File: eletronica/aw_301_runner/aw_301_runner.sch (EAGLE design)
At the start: 9 parts, among them IC1 AT90S2313P, Q1 4 Mhz

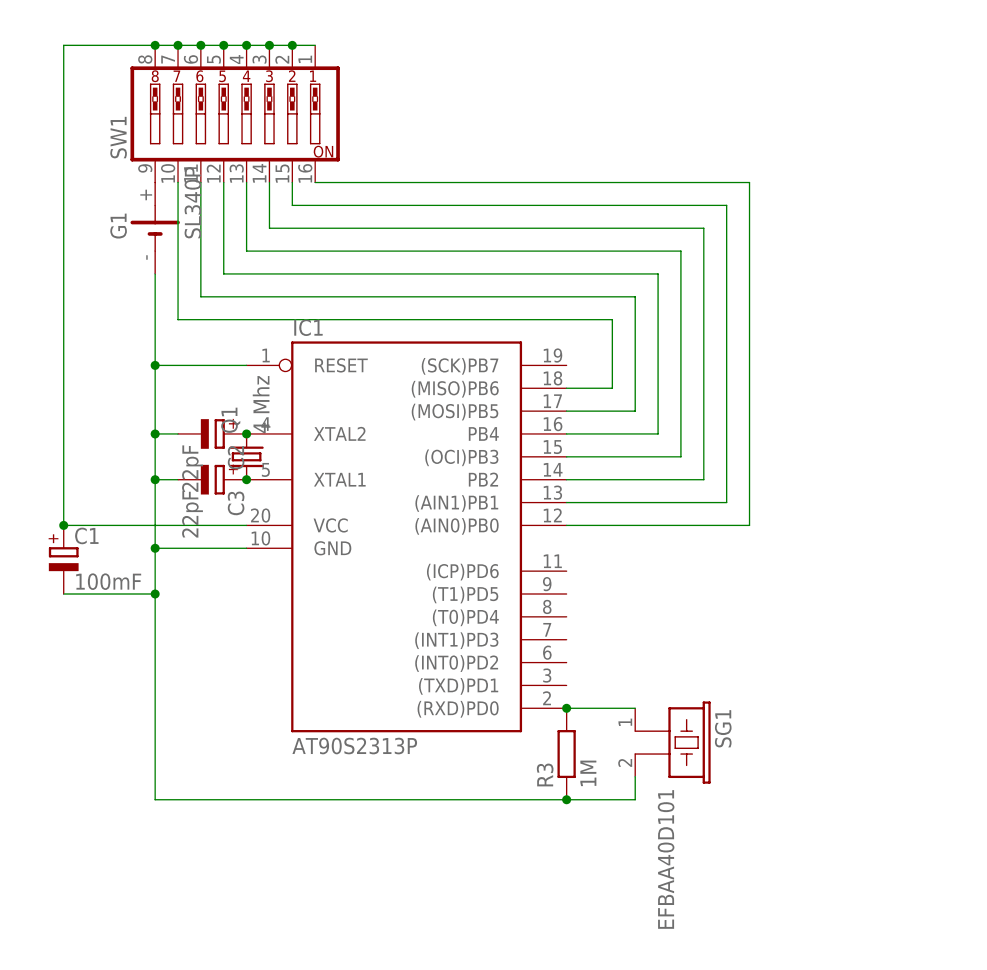
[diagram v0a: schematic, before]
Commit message: 
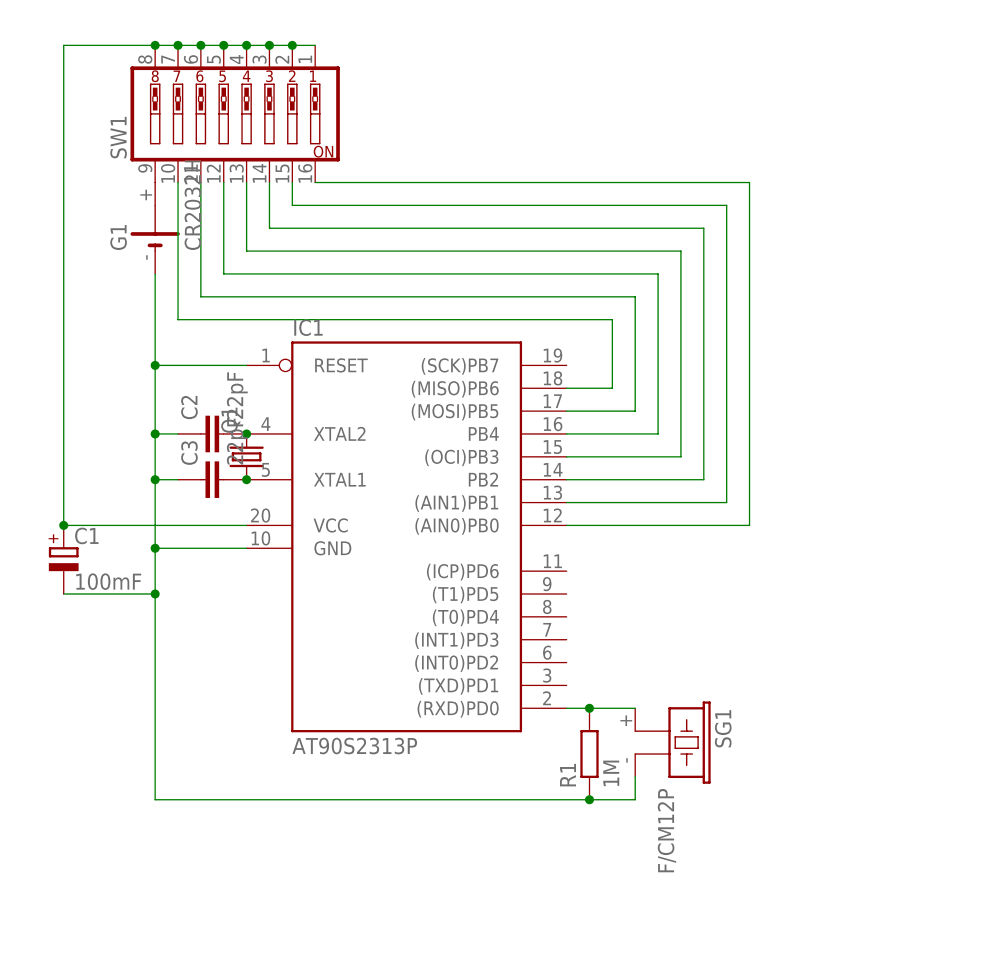
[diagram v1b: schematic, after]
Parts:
- removed R3: 1M, resistor:R-EU_0204/7
- added R1: 1M, rcl:R-EU_0207/10
- C1: device resistor:CPOL-EUE -> resistor:CPOL-EUE2.5-6
- C2, C3: device resistor:CPOL-EUE -> rcl:C-EU025-025X050
- G1: value SL340P -> CR2032H; device battery:SL340P -> battery:CR2032H
- Q1: value 4 Mhz -> (none); device crystal:CRYSTALHC49U-V -> crystal:CRYSTALHC49U70
- SG1: value EFBAA40D101 -> F/CM12P; device buzzer:EFBAA40D101 -> buzzer:F/CM12P
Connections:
- net N$2: now also C2.2; no longer C2.+
- net N$3: now also C3.2; no longer C3.+
- net N$6: now also R1.2; no longer R3.2
- net N$7: now also C2.1, C3.1, R1.1; no longer C2.-, C3.-, R3.1
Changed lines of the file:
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@@
 <part name="IC1" library="atmel" deviceset="AT90S2313" device="P"/>
 <part name="SW1" library="special" deviceset="SW_DIP-8" device=""/>
-<part name="G1" library="battery" deviceset="SL340P" device=""/>
-<part name="Q1" library="crystal" deviceset="CRYSTAL" device="HC49U-V" value="4 Mhz"/>
-<part name="C1" library="resistor" deviceset="CPOL-EU" device="E" value="100mF"/>
-<part name="R3" library="resistor" deviceset="R-EU_" device="0204/7" value="1M"/>
-<part name="SG1" library="buzzer" deviceset="EFB?" device="AA40D101"/>
-<part name="C2" library="resistor" deviceset="CPOL-EU" device="E" value="22pF"/>
-<part name="C3" library="resistor" deviceset="CPOL-EU" device="E" value="22pF"/>
+<part name="G1" library="battery" deviceset="CR2032H" device=""/>
+<part name="SG1" library="buzzer" deviceset="F/CM12P" device=""/>
+<part name="C1" library="resistor" deviceset="CPOL-EU" device="E2.5-6" value="100mF"/>
+<part name="Q1" library="crystal" deviceset="CRYSTAL" device="HC49U70"/>
+<part name="C2" library="rcl" deviceset="C-EU" device="025-025X050" value="22pF"/>
+<part name="C3" library="rcl" deviceset="C-EU" device="025-025X050" value="22pF"/>
+<part name="R1" library="rcl" deviceset="R-EU_" device="0207/10" value="1M"/>
 </parts>
 <sheets>
@@
 <instance part="IC1" gate="G$1" x="93.98" y="30.48"/>
 <instance part="SW1" gate="A" x="73.66" y="78.74" rot="R90"/>
-<instance part="G1" gate="G$1" x="66.04" y="66.04" rot="R90"/>
+<instance part="G1" gate="1" x="66.04" y="66.04" rot="R90"/>
+<instance part="SG1" gate="G$1" x="121.92" y="10.16" rot="R270"/>
+<instance part="C1" gate="G$1" x="55.88" y="30.48"/>
 <instance part="Q1" gate="G$1" x="76.2" y="40.64" rot="R90"/>
-<instance part="C1" gate="G$1" x="55.88" y="30.48"/>
-<instance part="R3" gate="G$1" x="111.76" y="7.62" rot="R90"/>
-<instance part="SG1" gate="G$1" x="121.92" y="10.16" rot="R270"/>
-<instance part="C2" gate="G$1" x="73.66" y="43.18" rot="R270"/>
-<instance part="C3" gate="G$1" x="73.66" y="38.1" rot="R270"/>
+<instance part="C2" gate="G$1" x="71.12" y="43.18" rot="R90"/>
+<instance part="C3" gate="G$1" x="71.12" y="38.1" rot="R90"/>
+<instance part="R1" gate="G$1" x="114.3" y="7.62" rot="R90"/>
 </instances>
 <busses>
 </busses>
 <nets>
-<net name="N$1" class="0">
-<segment>
-<pinref part="SW1" gate="A" pin="9"/>
-<pinref part="G1" gate="G$1" pin="+"/>
-</segment>
-</net>
 <net name="N$2" class="0">
 <segment>
 <pinref part="IC1" gate="G$1" pin="XTAL2"/>
+<junction x="76.2" y="43.18"/>
 <pinref part="Q1" gate="G$1" pin="2"/>
-<junction x="76.2" y="43.18"/>
-<pinref part="C2" gate="G$1" pin="+"/>
+<pinref part="C2" gate="G$1" pin="2"/>
 </segment>
 </net>
@@
 <segment>
 <pinref part="IC1" gate="G$1" pin="XTAL1"/>
+<junction x="76.2" y="38.1"/>
 <pinref part="Q1" gate="G$1" pin="1"/>
-<junction x="76.2" y="38.1"/>
-<pinref part="C3" gate="G$1" pin="+"/>
+<pinref part="C3" gate="G$1" pin="2"/>
 </segment>
 </net>
@@
 <pinref part="IC1" gate="G$1" pin="VCC"/>
 <wire x1="55.88" y1="33.02" x2="76.2" y2="33.02" width="0.1524" layer="91"/>
-<pinref part="C1" gate="G$1" pin="+"/>
-<junction x="55.88" y="33.02"/>
 <pinref part="SW1" gate="A" pin="7"/>
 <wire x1="66.04" y1="86.36" x2="68.58" y2="86.36" width="0.1524" layer="91"/>
@@
 <wire x1="81.28" y1="86.36" x2="83.82" y2="86.36" width="0.1524" layer="91"/>
 <junction x="81.28" y="86.36"/>
+<pinref part="C1" gate="G$1" pin="+"/>
+<junction x="55.88" y="33.02"/>
 </segment>
 </net>
@@
 <segment>
 <pinref part="IC1" gate="G$1" pin="(RXD)PD0"/>
-<pinref part="R3" gate="G$1" pin="2"/>
+<wire x1="111.76" y1="12.7" x2="114.3" y2="12.7" width="0.1524" layer="91"/>
 <pinref part="SG1" gate="G$1" pin="1"/>
-<wire x1="111.76" y1="12.7" x2="119.38" y2="12.7" width="0.1524" layer="91"/>
-<junction x="111.76" y="12.7"/>
+<pinref part="R1" gate="G$1" pin="2"/>
+<wire x1="114.3" y1="12.7" x2="119.38" y2="12.7" width="0.1524" layer="91"/>
+<junction x="114.3" y="12.7"/>
 </segment>
 </net>
 <net name="N$7" class="0">
 <segment>
-<pinref part="R3" gate="G$1" pin="1"/>
-<pinref part="SG1" gate="G$1" pin="2"/>
-<wire x1="111.76" y1="2.54" x2="119.38" y2="2.54" width="0.1524" layer="91"/>
 <wire x1="119.38" y1="2.54" x2="119.38" y2="5.08" width="0.1524" layer="91"/>
-<pinref part="G1" gate="G$1" pin="-"/>
 <pinref part="IC1" gate="G$1" pin="RESET"/>
 <wire x1="66.04" y1="60.96" x2="66.04" y2="50.8" width="0.1524" layer="91"/>
@@
 <wire x1="66.04" y1="38.1" x2="66.04" y2="30.48" width="0.1524" layer="91"/>
 <wire x1="66.04" y1="30.48" x2="76.2" y2="30.48" width="0.1524" layer="91"/>
-<pinref part="C1" gate="G$1" pin="-"/>
 <wire x1="55.88" y1="25.4" x2="66.04" y2="25.4" width="0.1524" layer="91"/>
 <wire x1="66.04" y1="25.4" x2="66.04" y2="30.48" width="0.1524" layer="91"/>
 <junction x="66.04" y="30.48"/>
-<wire x1="111.76" y1="2.54" x2="66.04" y2="2.54" width="0.1524" layer="91"/>
+<wire x1="119.38" y1="2.54" x2="114.3" y2="2.54" width="0.1524" layer="91"/>
+<wire x1="114.3" y1="2.54" x2="66.04" y2="2.54" width="0.1524" layer="91"/>
 <wire x1="66.04" y1="2.54" x2="66.04" y2="25.4" width="0.1524" layer="91"/>
-<junction x="111.76" y="2.54"/>
 <junction x="66.04" y="25.4"/>
-<pinref part="C2" gate="G$1" pin="-"/>
 <wire x1="68.58" y1="43.18" x2="66.04" y2="43.18" width="0.1524" layer="91"/>
 <junction x="66.04" y="43.18"/>
-<pinref part="C3" gate="G$1" pin="-"/>
 <wire x1="68.58" y1="38.1" x2="66.04" y2="38.1" width="0.1524" layer="91"/>
 <junction x="66.04" y="38.1"/>
+<pinref part="G1" gate="1" pin="-"/>
+<pinref part="SG1" gate="G$1" pin="2"/>
+<pinref part="C1" gate="G$1" pin="-"/>
+<pinref part="C2" gate="G$1" pin="1"/>
+<pinref part="C3" gate="G$1" pin="1"/>
+<pinref part="R1" gate="G$1" pin="1"/>
+<junction x="114.3" y="2.54"/>
 </segment>
 </net>
@@
 </segment>
 </net>
+<net name="N$1" class="0">
+<segment>
+<pinref part="SW1" gate="A" pin="9"/>
+<pinref part="G1" gate="1" pin="+"/>
+</segment>
+</net>

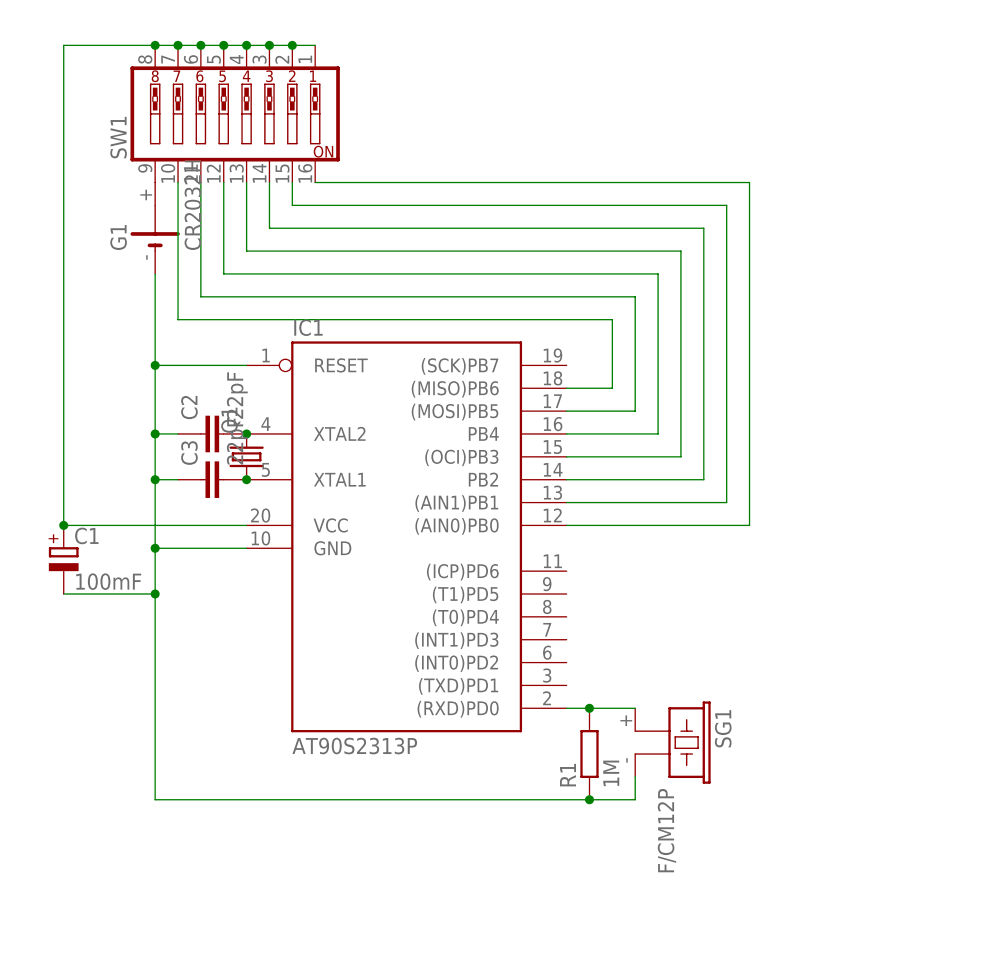
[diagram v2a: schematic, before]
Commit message: 
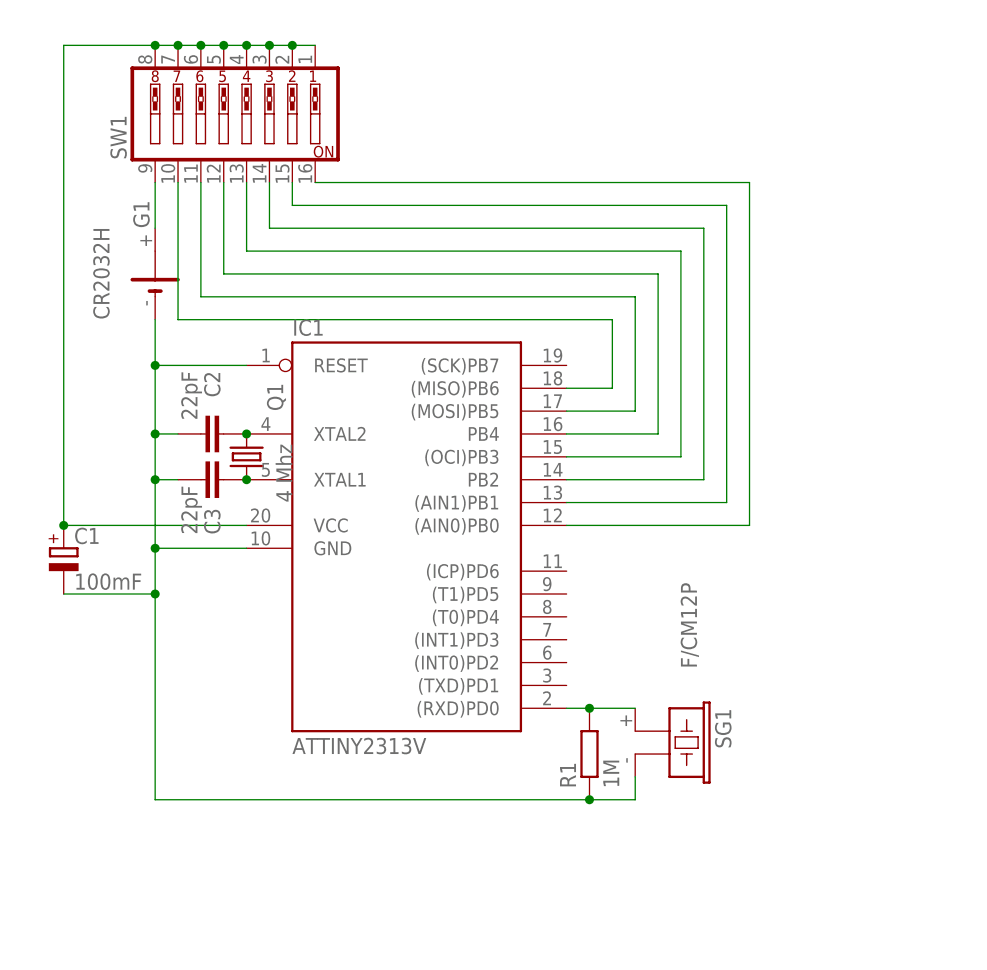
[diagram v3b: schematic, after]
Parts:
- IC1: value AT90S2313P -> ATTINY2313V
- Q1: value (none) -> 4 Mhz
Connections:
- net N$5 renamed VCC
- net N$7 renamed GND
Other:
- moved on the sheet: G1
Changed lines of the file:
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@@
 <grid distance="0.1" unitdist="inch" unit="inch" style="lines" multiple="1" display="no" altdistance="0.01" altunitdist="inch" altunit="inch"/>
 <layers>
-<layer number="1" name="Top" color="4" fill="1" visible="no" active="no"/>
-<layer number="16" name="Bottom" color="1" fill="1" visible="no" active="no"/>
-<layer number="17" name="Pads" color="2" fill="1" visible="no" active="no"/>
-<layer number="18" name="Vias" color="2" fill="1" visible="no" active="no"/>
-<layer number="19" name="Unrouted" color="6" fill="1" visible="no" active="no"/>
-<layer number="20" name="Dimension" color="15" fill="1" visible="no" active="no"/>
-<layer number="21" name="tPlace" color="7" fill="1" visible="no" active="no"/>
-<layer number="22" name="bPlace" color="7" fill="1" visible="no" active="no"/>
-<layer number="23" name="tOrigins" color="15" fill="1" visible="no" active="no"/>
-<layer number="24" name="bOrigins" color="15" fill="1" visible="no" active="no"/>
-<layer number="25" name="tNames" color="7" fill="1" visible="no" active="no"/>
-<layer number="26" name="bNames" color="7" fill="1" visible="no" active="no"/>
-<layer number="27" name="tValues" color="7" fill="1" visible="no" active="no"/>
-<layer number="28" name="bValues" color="7" fill="1" visible="no" active="no"/>
+<layer number="1" name="Top" color="4" fill="1" visible="yes" active="no"/>
+<layer number="16" name="Bottom" color="1" fill="1" visible="yes" active="no"/>
+<layer number="17" name="Pads" color="2" fill="1" visible="yes" active="no"/>
+<layer number="18" name="Vias" color="2" fill="1" visible="yes" active="no"/>
+<layer number="19" name="Unrouted" color="6" fill="1" visible="yes" active="no"/>
+<layer number="20" name="Dimension" color="15" fill="1" visible="yes" active="no"/>
+<layer number="21" name="tPlace" color="7" fill="1" visible="yes" active="no"/>
+<layer number="22" name="bPlace" color="7" fill="1" visible="yes" active="no"/>
+<layer number="23" name="tOrigins" color="15" fill="1" visible="yes" active="no"/>
+<layer number="24" name="bOrigins" color="15" fill="1" visible="yes" active="no"/>
+<layer number="25" name="tNames" color="7" fill="1" visible="yes" active="no"/>
+<layer number="26" name="bNames" color="7" fill="1" visible="yes" active="no"/>
+<layer number="27" name="tValues" color="7" fill="1" visible="yes" active="no"/>
+<layer number="28" name="bValues" color="7" fill="1" visible="yes" active="no"/>
 <layer number="29" name="tStop" color="7" fill="3" visible="no" active="no"/>
 <layer number="30" name="bStop" color="7" fill="6" visible="no" active="no"/>
@@
 <layer number="35" name="tGlue" color="7" fill="4" visible="no" active="no"/>
 <layer number="36" name="bGlue" color="7" fill="5" visible="no" active="no"/>
-<layer number="37" name="tTest" color="7" fill="1" visible="no" active="no"/>
-<layer number="38" name="bTest" color="7" fill="1" visible="no" active="no"/>
+<layer number="37" name="tTest" color="7" fill="1" visible="yes" active="no"/>
+<layer number="38" name="bTest" color="7" fill="1" visible="yes" active="no"/>
 <layer number="39" name="tKeepout" color="4" fill="11" visible="no" active="no"/>
 <layer number="40" name="bKeepout" color="1" fill="11" visible="no" active="no"/>
@@
 <layer number="44" name="Drills" color="7" fill="1" visible="no" active="no"/>
 <layer number="45" name="Holes" color="7" fill="1" visible="no" active="no"/>
-<layer number="46" name="Milling" color="3" fill="1" visible="no" active="no"/>
-<layer number="47" name="Measures" color="7" fill="1" visible="no" active="no"/>
-<layer number="48" name="Document" color="7" fill="1" visible="no" active="no"/>
-<layer number="49" name="Reference" color="7" fill="1" visible="no" active="no"/>
-<layer number="51" name="tDocu" color="6" fill="9" visible="no" active="no"/>
-<layer number="52" name="bDocu" color="7" fill="1" visible="no" active="no"/>
+<layer number="46" name="Milling" color="3" fill="1" visible="yes" active="no"/>
+<layer number="47" name="Measures" color="7" fill="1" visible="yes" active="no"/>
+<layer number="48" name="Document" color="7" fill="1" visible="yes" active="no"/>
+<layer number="49" name="Reference" color="7" fill="1" visible="yes" active="no"/>
+<layer number="51" name="tDocu" color="7" fill="1" visible="yes" active="no"/>
+<layer number="52" name="bDocu" color="7" fill="1" visible="yes" active="no"/>
 <layer number="91" name="Nets" color="2" fill="1" visible="yes" active="yes"/>
 <layer number="92" name="Busses" color="1" fill="1" visible="yes" active="yes"/>
@@
 <classes>
 <class number="0" name="default" width="1.27" drill="0">
-<clearance class="0" value="0.508"/>
+<clearance class="0" value="0.762"/>
 </class>
 </classes>
 <parts>
-<part name="IC1" library="atmel" deviceset="AT90S2313" device="P"/>
+<part name="IC1" library="atmel" deviceset="AT90S2313" device="P" value="ATTINY2313V"/>
 <part name="SW1" library="special" deviceset="SW_DIP-8" device=""/>
 <part name="G1" library="battery" deviceset="CR2032H" device=""/>
 <part name="SG1" library="buzzer" deviceset="F/CM12P" device=""/>
 <part name="C1" library="resistor" deviceset="CPOL-EU" device="E2.5-6" value="100mF"/>
-<part name="Q1" library="crystal" deviceset="CRYSTAL" device="HC49U70"/>
+<part name="Q1" library="crystal" deviceset="CRYSTAL" device="HC49U70" value="4 Mhz"/>
 <part name="C2" library="rcl" deviceset="C-EU" device="025-025X050" value="22pF"/>
 <part name="C3" library="rcl" deviceset="C-EU" device="025-025X050" value="22pF"/>
@@
 <instance part="IC1" gate="G$1" x="93.98" y="30.48"/>
 <instance part="SW1" gate="A" x="73.66" y="78.74" rot="R90"/>
-<instance part="G1" gate="1" x="66.04" y="66.04" rot="R90"/>
-<instance part="SG1" gate="G$1" x="121.92" y="10.16" rot="R270"/>
+<instance part="G1" gate="1" x="66.04" y="60.96" smashed="yes" rot="R90">
+<attribute name="NAME" x="65.405" y="66.04" size="1.778" layer="95" rot="R90"/>
+<attribute name="VALUE" x="60.96" y="55.88" size="1.778" layer="96" rot="R90"/>
+</instance>
+<instance part="SG1" gate="G$1" x="121.92" y="10.16" smashed="yes" rot="R270">
+<attribute name="NAME" x="128.27" y="12.7" size="1.778" layer="95" rot="R270"/>
+<attribute name="VALUE" x="124.46" y="26.67" size="1.778" layer="96" rot="R270"/>
+</instance>
 <instance part="C1" gate="G$1" x="55.88" y="30.48"/>
-<instance part="Q1" gate="G$1" x="76.2" y="40.64" rot="R90"/>
-<instance part="C2" gate="G$1" x="71.12" y="43.18" rot="R90"/>
-<instance part="C3" gate="G$1" x="71.12" y="38.1" rot="R90"/>
+<instance part="Q1" gate="G$1" x="76.2" y="40.64" smashed="yes" rot="R90">
+<attribute name="NAME" x="80.264" y="45.72" size="1.778" layer="95" rot="R90"/>
+<attribute name="VALUE" x="81.28" y="35.56" size="1.778" layer="96" rot="R90"/>
+</instance>
+<instance part="C2" gate="G$1" x="71.12" y="43.18" smashed="yes" rot="R90">
+<attribute name="NAME" x="73.279" y="47.244" size="1.778" layer="95" rot="R90"/>
+<attribute name="VALUE" x="70.739" y="44.704" size="1.778" layer="96" rot="R90"/>
+</instance>
+<instance part="C3" gate="G$1" x="71.12" y="38.1" smashed="yes" rot="R90">
+<attribute name="NAME" x="73.279" y="32.004" size="1.778" layer="95" rot="R90"/>
+<attribute name="VALUE" x="70.739" y="32.004" size="1.778" layer="96" rot="R90"/>
+</instance>
 <instance part="R1" gate="G$1" x="114.3" y="7.62" rot="R90"/>
 </instances>
@@
 </segment>
 </net>
-<net name="N$5" class="0">
+<net name="VCC" class="0">
 <segment>
 <pinref part="SW1" gate="A" pin="8"/>
@@
 </segment>
 </net>
-<net name="N$7" class="0">
+<net name="GND" class="0">
 <segment>
 <wire x1="119.38" y1="2.54" x2="119.38" y2="5.08" width="0.1524" layer="91"/>
 <pinref part="IC1" gate="G$1" pin="RESET"/>
-<wire x1="66.04" y1="60.96" x2="66.04" y2="50.8" width="0.1524" layer="91"/>
+<wire x1="66.04" y1="55.88" x2="66.04" y2="50.8" width="0.1524" layer="91"/>
 <wire x1="66.04" y1="50.8" x2="76.2" y2="50.8" width="0.1524" layer="91"/>
 <wire x1="66.04" y1="50.8" x2="66.04" y2="43.18" width="0.1524" layer="91"/>
@@
 <pinref part="SW1" gate="A" pin="9"/>
 <pinref part="G1" gate="1" pin="+"/>
-</segment>
-</net>
+<wire x1="66.04" y1="66.04" x2="66.04" y2="71.12" width="0.1524" layer="91"/>
+</segment>
+</net>
